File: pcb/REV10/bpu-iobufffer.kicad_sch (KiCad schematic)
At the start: 36 parts, among them J301 Conn_01x10, J302 Conn_01x09, U301 SN74LVC1T45DCK, U302 SN74LVC1T45DCK, U303 SN74LVC1T45DCK, U304 SN74LVC1T45DCK, U305 SN74LVC1T45DCK, U306 SN74LVC1T45DCK, U307 SN74LVC1T45DCK, U308 SN74LVC1T45DCK

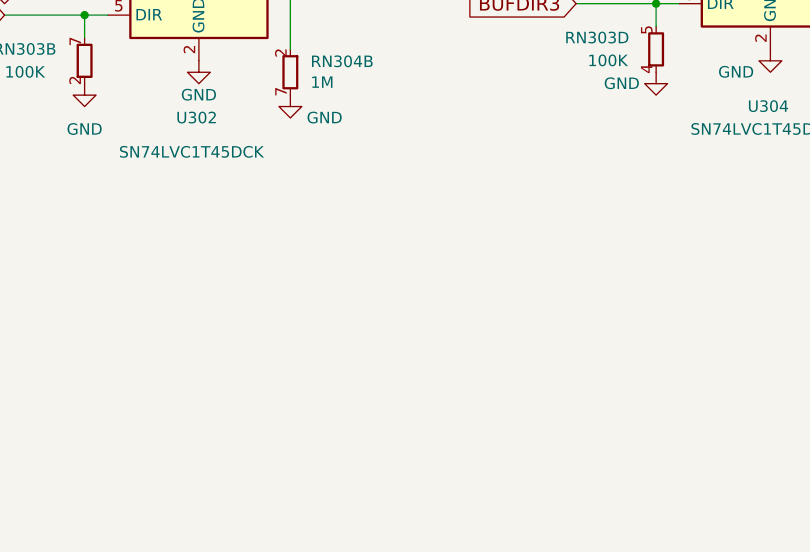
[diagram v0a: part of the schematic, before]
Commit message: Add pulldown on VREF. Change VUSB MUX series resistor to 510R. May be other value updates that didn't get checked in previously.
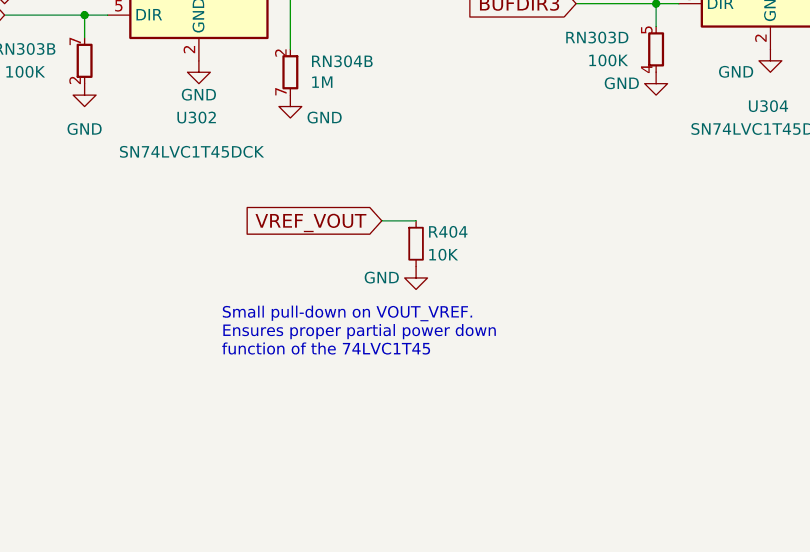
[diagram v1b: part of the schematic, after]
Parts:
- added R404: 10K, Resistor_SMD:R_0402_1005Metric, symbol Device:R_Small
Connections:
- net GND: now also R404.2
- net VREF_VOUT: now also R404.1
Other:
- note added: "Small pull-down on VOUT_VREF. Ensures proper partial power down function of the 74LVC1T45"
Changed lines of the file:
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@@
     (stroke (width 0) (type default))
   )
+  (wire (pts (xy 69.85 125.73) (xy 73.66 125.73))
+    (stroke (width 0) (type default))
+  )
   (wire (pts (xy 102.87 40.64) (xy 100.33 40.64))
     (stroke (width 0) (type default))
@@
     (stroke (width 0) (type default))
   )
+  (text "Small pull-down on VOUT_VREF.\nEnsures proper partial power down \nfunction of the 74LVC1T45"
+    (at 52.07 140.97 0)
+    (effects (font (size 1.27 1.27)) (justify left bottom))
+  )
   (text "BUS PIRATE I/O" (at 242.57 160.02 0)
     (effects (font (size 1.524 1.524)) (justify right bottom))
@@
     )
   )
+  (global_label "VREF_VOUT" (shape input) (at 69.85 125.73 180)
+    (effects (font (size 1.524 1.524)) (justify right))
+    (property "Intersheetrefs" "${INTERSHEET_REFS}" (at 69.85 125.73 0)
+      (effects (font (size 1.27 1.27)) hide)
+    )
+  )
   (global_label "BPIO6" (shape input) (at 234.95 147.32 180)
     (effects (font (size 1.27 1.27)) (justify right))
@@
         )
       )
+    )
+  )
+  (symbol (lib_id "power:GND") (at 73.66 130.81 0) (unit 1)
+    (in_bom yes) (on_board yes) (dnp no)
+    (property "Reference" "#PWR016" (at 73.66 137.16 0)
+      (effects (font (size 1.27 1.27)) hide)
+    )
+    (property "Value" "GND" (at 69.85 132.08 0)
+      (effects (font (size 1.27 1.27)))
+    )
+    (property "Footprint" "" (at 73.66 130.81 0)
+      (effects (font (size 1.27 1.27)) hide)
+    )
+    (property "Datasheet" "" (at 73.66 130.81 0)
+      (effects (font (size 1.27 1.27)) hide)
+    )
+    (pin "1")
+    (instances
+      (project "BusPirate-5-rev10"
+        (path "/1f56410a-eaac-4444-b0f7-cfd3531e22ac/00000000-0000-0000-0000-00005f344f30"
+          (reference "#PWR016") (unit 1)
+        )
+      )
+    )
+  )
+  (symbol (lib_id "Device:R_Small") (at 73.66 128.27 0) (unit 1)
+    (in_bom yes) (on_board yes) (dnp no)
+    (property "Reference" "R404" (at 74.93 127 0)
+      (effects (font (size 1.27 1.27)) (justify left))
+    )
+    (property "Value" "10K" (at 74.93 129.54 0)
+      (effects (font (size 1.27 1.27)) (justify left))
+    )
+    (property "Footprint" "Resistor_SMD:R_0402_1005Metric" (at 73.66 128.27 0)
+      (effects (font (size 1.27 1.27)) hide)
+    )
+    (property "Datasheet" "~" (at 73.66 128.27 0)
+      (effects (font (size 1.27 1.27)) hide)
+    )
+    (property "RMB" "0.005749" (at 73.66 128.27 0)
+      (effects (font (size 1.27 1.27)) hide)
+    )
+    (property "Supplier" "https://item.szlcsc.com/61543.html" (at 73.66 128.27 0)
+      (effects (font (size 1.27 1.27)) hide)
+    )
+    (pin "1")
+    (pin "2")
+    (instances
+      (project "BusPirate-5-rev10"
+        (path "/1f56410a-eaac-4444-b0f7-cfd3531e22ac/00000000-0000-0000-0000-00005f46fad3"
+          (reference "R404") (unit 1)
+        )
+        (path "/1f56410a-eaac-4444-b0f7-cfd3531e22ac/00000000-0000-0000-0000-00005f344f30"
+          (reference "R301") (unit 1)
+        )
+      )

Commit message: rev10 pcb
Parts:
- U301, U302, U303, U304, U305, U306, U307, U308: value SN74LVC1T45DCK -> 74LVC1T45
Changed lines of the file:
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@@
       (effects (font (size 1.27 1.27)) (justify left))
     )
-    (property "Value" "SN74LVC1T45DCK" (at 40.64 118.11 0)
+    (property "Value" "74LVC1T45" (at 40.64 118.11 0)
       (effects (font (size 1.27 1.27)) (justify left))
     )
@@
       (effects (font (size 1.27 1.27)) (justify left))
     )
-    (property "Value" "SN74LVC1T45DCK" (at 105.41 60.96 0)
+    (property "Value" "74LVC1T45" (at 105.41 60.96 0)
       (effects (font (size 1.27 1.27)) (justify left))
     )
@@
       (effects (font (size 1.27 1.27)) (justify left))
     )
-    (property "Value" "SN74LVC1T45DCK" (at 104.14 115.57 0)
+    (property "Value" "74LVC1T45" (at 104.14 115.57 0)
       (effects (font (size 1.27 1.27)) (justify left))
     )
@@
       (effects (font (size 1.27 1.27)) (justify left))
     )
-    (property "Value" "SN74LVC1T45DCK" (at 242.57 110.49 0)
+    (property "Value" "74LVC1T45" (at 242.57 110.49 0)
       (effects (font (size 1.27 1.27)) (justify left))
     )
@@
       (effects (font (size 1.27 1.27)) (justify left))
     )
-    (property "Value" "SN74LVC1T45DCK" (at 245.11 60.96 0)
+    (property "Value" "74LVC1T45" (at 245.11 60.96 0)
       (effects (font (size 1.27 1.27)) (justify left))
     )
@@
       (effects (font (size 1.27 1.27)) (justify left))
     )
-    (property "Value" "SN74LVC1T45DCK" (at 171.45 114.3 0)
+    (property "Value" "74LVC1T45" (at 171.45 114.3 0)
       (effects (font (size 1.27 1.27)) (justify left))
     )
@@
       (effects (font (size 1.27 1.27)) (justify left))
     )
-    (property "Value" "SN74LVC1T45DCK" (at 173.99 60.96 0)
+    (property "Value" "74LVC1T45" (at 173.99 60.96 0)
       (effects (font (size 1.27 1.27)) (justify left))
     )
@@
       (effects (font (size 1.27 1.27)) (justify left))
     )
-    (property "Value" "SN74LVC1T45DCK" (at 40.64 60.96 0)
+    (property "Value" "74LVC1T45" (at 40.64 60.96 0)
       (effects (font (size 1.27 1.27)) (justify left))
     )
